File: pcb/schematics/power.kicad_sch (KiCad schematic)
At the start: 0 parts

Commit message: add more components
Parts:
- added U?: LP3853ESX-3.3/NOPB, VREG_TPS79625KTTR, symbol LP3853ESX-3.3_NOPB:LP3853ESX-3.3/NOPB
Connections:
- new net: U?.3 (GND), U?.6 (GND)
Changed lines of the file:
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@@
 (kicad_sch (version 20220126) (generator eeschema)
   (paper "A4")
+  (symbol (lib_id "LP3853ESX-3.3_NOPB:LP3853ESX-3.3{slash}NOPB") (at 148.59 86.36 0) (unit 1)
+    (in_bom yes) (on_board yes) (fields_autoplaced)
+    (property "Reference" "U?" (id 0) (at 148.59 72.39 0)
+      (effects (font (size 1.27 1.27)))
+    )
+    (property "Value" "LP3853ESX-3.3/NOPB" (id 1) (at 148.59 74.93 0)
+      (effects (font (size 1.27 1.27)))
+    )
+    (property "Footprint" "VREG_TPS79625KTTR" (id 2) (at 148.59 86.36 0)
+      (effects (font (size 1.27 1.27)) (justify left bottom) hide)
+    )
+    (property "Datasheet" "https://www.ti.com/lit/ds/symlink/lp3853.pdf?HQS=dis-mous-null-mousermode-dsf-pf-null-wwe&ts=1634641603473&ref_url=https%253A%252F%252Fcz.mouser.com%252F" (id 3) (at 148.59 86.36 0)
+      (effects (font (size 1.27 1.27)) (justify left bottom) hide)
+    )
+    (pin "1")
+    (pin "2")
+    (pin "3")
+    (pin "4")
+    (pin "5")
+    (pin "6")
+  )
 )

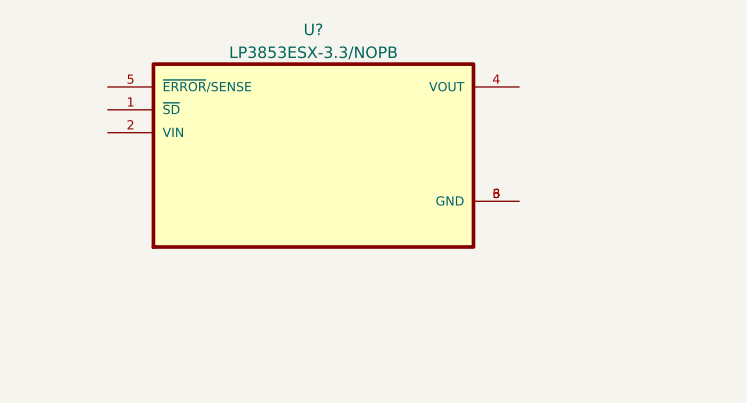
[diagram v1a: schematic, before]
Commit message: add architecture diagramé
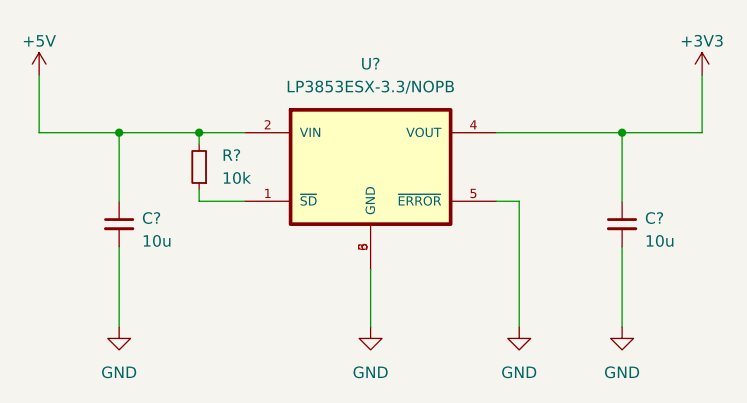
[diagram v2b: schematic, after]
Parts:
- added C? (x2): 10u, symbol Device:C_Small
- added R?: 10k, symbol Device:R_Small
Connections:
- net at U?.1 (~{SD}): now also R?.1
- net +5V: now reaches U?.2 (VIN)
- net +5V: now also C?.1, R?.2
- net GND: now reaches U?.3 (GND), U?.6 (GND)
- net GND: now also U?.5 (~{ERROR}), C?.2, C?.2
- net +3V3: now reaches U?.4 (VOUT)
- net +3V3: now also C?.1
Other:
- moved on the sheet: U?
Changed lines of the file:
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@@
 (kicad_sch (version 20220126) (generator eeschema)
   (paper "A4")
-  (symbol (lib_id "LP3853ESX-3.3_NOPB:LP3853ESX-3.3{slash}NOPB") (at 148.59 86.36 0) (unit 1)
-    (in_bom yes) (on_board yes) (fields_autoplaced)
-    (property "Reference" "U?" (id 0) (at 148.59 72.39 0)
-      (effects (font (size 1.27 1.27)))
-    )
-    (property "Value" "LP3853ESX-3.3/NOPB" (id 1) (at 148.59 74.93 0)
-      (effects (font (size 1.27 1.27)))
-    )
-    (property "Footprint" "VREG_TPS79625KTTR" (id 2) (at 148.59 86.36 0)
+  (junction (at 182.88 83.82) (diameter 0) (color 0 0 0 0)
+  )
+  (junction (at 135.89 83.82) (diameter 0) (color 0 0 0 0)
+  )
+  (junction (at 127 83.82) (diameter 0) (color 0 0 0 0)
+  )
+  (wire (pts (xy 182.88 83.82) (xy 182.88 91.44))
+    (stroke (width 0) (type default))
+  )
+  (wire (pts (xy 191.77 83.82) (xy 191.77 77.47))
+    (stroke (width 0) (type default))
+  )
+  (wire (pts (xy 118.11 77.47) (xy 118.11 83.82))
+    (stroke (width 0) (type default))
+  )
+  (wire (pts (xy 127 96.52) (xy 127 105.41))
+    (stroke (width 0) (type default))
+  )
+  (wire (pts (xy 118.11 83.82) (xy 127 83.82))
+    (stroke (width 0) (type default))
+  )
+  (wire (pts (xy 135.89 83.82) (xy 135.89 85.09))
+    (stroke (width 0) (type default))
+  )
+  (wire (pts (xy 171.45 105.41) (xy 171.45 91.44))
+    (stroke (width 0) (type default))
+  )
+  (wire (pts (xy 171.45 91.44) (xy 168.91 91.44))
+    (stroke (width 0) (type default))
+  )
+  (wire (pts (xy 182.88 96.52) (xy 182.88 105.41))
+    (stroke (width 0) (type default))
+  )
+  (wire (pts (xy 127 83.82) (xy 135.89 83.82))
+    (stroke (width 0) (type default))
+  )
+  (wire (pts (xy 140.97 91.44) (xy 135.89 91.44))
+    (stroke (width 0) (type default))
+  )
+  (wire (pts (xy 135.89 91.44) (xy 135.89 90.17))
+    (stroke (width 0) (type default))
+  )
+  (wire (pts (xy 168.91 83.82) (xy 182.88 83.82))
+    (stroke (width 0) (type default))
+  )
+  (wire (pts (xy 127 83.82) (xy 127 91.44))
+    (stroke (width 0) (type default))
+  )
+  (wire (pts (xy 182.88 83.82) (xy 191.77 83.82))
+    (stroke (width 0) (type default))
+  )
+  (wire (pts (xy 135.89 83.82) (xy 140.97 83.82))
+    (stroke (width 0) (type default))
+  )
+  (wire (pts (xy 154.94 99.06) (xy 154.94 105.41))
+    (stroke (width 0) (type default))
+  )
+  (symbol (lib_id "power:GND") (at 127 105.41 0) (unit 1)
+    (in_bom yes) (on_board yes) (fields_autoplaced)
+    (property "Reference" "#PWR?" (id 0) (at 127 111.76 0)
+      (effects (font (size 1.27 1.27)) hide)
+    )
+    (property "Value" "GND" (id 1) (at 127 110.49 0)
+      (effects (font (size 1.27 1.27)))
+    )
+    (property "Footprint" "" (id 2) (at 127 105.41 0)
+      (effects (font (size 1.27 1.27)) hide)
+    )
+    (property "Datasheet" "" (id 3) (at 127 105.41 0)
+      (effects (font (size 1.27 1.27)) hide)
+    )
+    (pin "1")
+  )
+  (symbol (lib_id "power:+5V") (at 118.11 77.47 0) (unit 1)
+    (in_bom yes) (on_board yes) (fields_autoplaced)
+    (property "Reference" "#PWR?" (id 0) (at 118.11 81.28 0)
+      (effects (font (size 1.27 1.27)) hide)
+    )
+    (property "Value" "+5V" (id 1) (at 118.11 73.66 0)
+      (effects (font (size 1.27 1.27)))
+    )
+    (property "Footprint" "" (id 2) (at 118.11 77.47 0)
+      (effects (font (size 1.27 1.27)) hide)
+    )
+    (property "Datasheet" "" (id 3) (at 118.11 77.47 0)
+      (effects (font (size 1.27 1.27)) hide)
+    )
+    (pin "1")
+  )
+  (symbol (lib_id "power:+3V3") (at 191.77 77.47 0) (unit 1)
+    (in_bom yes) (on_board yes) (fields_autoplaced)
+    (property "Reference" "#PWR?" (id 0) (at 191.77 81.28 0)
+      (effects (font (size 1.27 1.27)) hide)
+    )
+    (property "Value" "+3V3" (id 1) (at 191.77 73.66 0)
+      (effects (font (size 1.27 1.27)))
+    )
+    (property "Footprint" "" (id 2) (at 191.77 77.47 0)
+      (effects (font (size 1.27 1.27)) hide)
+    )
+    (property "Datasheet" "" (id 3) (at 191.77 77.47 0)
+      (effects (font (size 1.27 1.27)) hide)
+    )
+    (pin "1")
+  )
+  (symbol (lib_id "LP3853ESX-3.3_NOPB:LP3853ESX-3.3{slash}NOPB") (at 163.83 91.44 0) (unit 1)
+    (in_bom yes) (on_board yes)
+    (property "Reference" "U?" (id 0) (at 154.94 76.2 0)
+      (effects (font (size 1.27 1.27)))
+    )
+    (property "Value" "LP3853ESX-3.3/NOPB" (id 1) (at 154.94 78.74 0)
+      (effects (font (size 1.27 1.27)))
+    )
+    (property "Footprint" "VREG_TPS79625KTTR" (id 2) (at 163.83 91.44 0)
       (effects (font (size 1.27 1.27)) (justify left bottom) hide)
     )
-    (property "Datasheet" "https://www.ti.com/lit/ds/symlink/lp3853.pdf?HQS=dis-mous-null-mousermode-dsf-pf-null-wwe&ts=1634641603473&ref_url=https%253A%252F%252Fcz.mouser.com%252F" (id 3) (at 148.59 86.36 0)
+    (property "Datasheet" "https://www.ti.com/lit/ds/symlink/lp3853.pdf?HQS=dis-mous-null-mousermode-dsf-pf-null-wwe&ts=1634641603473&ref_url=https%253A%252F%252Fcz.mouser.com%252F" (id 3) (at 163.83 91.44 0)
       (effects (font (size 1.27 1.27)) (justify left bottom) hide)
     )
@@
     (pin "6")
   )
+  (symbol (lib_id "power:GND") (at 171.45 105.41 0) (unit 1)
+    (in_bom yes) (on_board yes) (fields_autoplaced)
+    (property "Reference" "#PWR?" (id 0) (at 171.45 111.76 0)
+      (effects (font (size 1.27 1.27)) hide)
+    )
+    (property "Value" "GND" (id 1) (at 171.45 110.49 0)
+      (effects (font (size 1.27 1.27)))
+    )
+    (property "Footprint" "" (id 2) (at 171.45 105.41 0)
+      (effects (font (size 1.27 1.27)) hide)
+    )
+    (property "Datasheet" "" (id 3) (at 171.45 105.41 0)
+      (effects (font (size 1.27 1.27)) hide)
+    )
+    (pin "1")
+  )
+  (symbol (lib_id "Device:C_Small") (at 127 93.98 0) (unit 1)
+    (in_bom yes) (on_board yes) (fields_autoplaced)
+    (property "Reference" "C?" (id 0) (at 129.54 93.3513 0)
+      (effects (font (size 1.27 1.27)) (justify left))
+    )
+    (property "Value" "10u" (id 1) (at 129.54 95.8913 0)
+      (effects (font (size 1.27 1.27)) (justify left))
+    )
+    (property "Footprint" "" (id 2) (at 127 93.98 0)
+      (effects (font (size 1.27 1.27)) hide)
+    )
+    (property "Datasheet" "~" (id 3) (at 127 93.98 0)
+      (effects (font (size 1.27 1.27)) hide)
+    )
+    (pin "1")
+    (pin "2")
+  )
+  (symbol (lib_id "Device:R_Small") (at 135.89 87.63 180) (unit 1)
+    (in_bom yes) (on_board yes)
+    (property "Reference" "R?" (id 0) (at 138.43 86.36 0)
+      (effects (font (size 1.27 1.27)) (justify right))
+    )
+    (property "Value" "10k" (id 1) (at 138.43 88.9 0)
+      (effects (font (size 1.27 1.27)) (justify right))
+    )
+    (property "Footprint" "" (id 2) (at 135.89 87.63 0)
+      (effects (font (size 1.27 1.27)) hide)
+    )
+    (property "Datasheet" "~" (id 3) (at 135.89 87.63 0)
+      (effects (font (size 1.27 1.27)) hide)
+    )
+    (pin "1")
+    (pin "2")
+  )
+  (symbol (lib_id "power:GND") (at 154.94 105.41 0) (unit 1)
+    (in_bom yes) (on_board yes) (fields_autoplaced)
+    (property "Reference" "#PWR?" (id 0) (at 154.94 111.76 0)
+      (effects (font (size 1.27 1.27)) hide)
+    )
+    (property "Value" "GND" (id 1) (at 154.94 110.49 0)
+      (effects (font (size 1.27 1.27)))
+    )
+    (property "Footprint" "" (id 2) (at 154.94 105.41 0)
+      (effects (font (size 1.27 1.27)) hide)
+    )
+    (property "Datasheet" "" (id 3) (at 154.94 105.41 0)
+      (effects (font (size 1.27 1.27)) hide)
+    )
+    (pin "1")
+  )
+  (symbol (lib_id "Device:C_Small") (at 182.88 93.98 0) (unit 1)
+    (in_bom yes) (on_board yes) (fields_autoplaced)
+    (property "Reference" "C?" (id 0) (at 185.42 93.3513 0)
+      (effects (font (size 1.27 1.27)) (justify left))
+    )
+    (property "Value" "10u" (id 1) (at 185.42 95.8913 0)
+      (effects (font (size 1.27 1.27)) (justify left))
+    )
+    (property "Footprint" "" (id 2) (at 182.88 93.98 0)
+      (effects (font (size 1.27 1.27)) hide)
+    )
+    (property "Datasheet" "~" (id 3) (at 182.88 93.98 0)
+      (effects (font (size 1.27 1.27)) hide)
+    )
+    (pin "1")
+    (pin "2")
+  )
+  (symbol (lib_id "power:GND") (at 182.88 105.41 0) (unit 1)
+    (in_bom yes) (on_board yes) (fields_autoplaced)
+    (property "Reference" "#PWR?" (id 0) (at 182.88 111.76 0)
+      (effects (font (size 1.27 1.27)) hide)
+    )
+    (property "Value" "GND" (id 1) (at 182.88 110.49 0)
+      (effects (font (size 1.27 1.27)))
+    )
+    (property "Footprint" "" (id 2) (at 182.88 105.41 0)
+      (effects (font (size 1.27 1.27)) hide)
+    )
+    (property "Datasheet" "" (id 3) (at 182.88 105.41 0)
+      (effects (font (size 1.27 1.27)) hide)
+    )
+    (pin "1")
+  )
 )

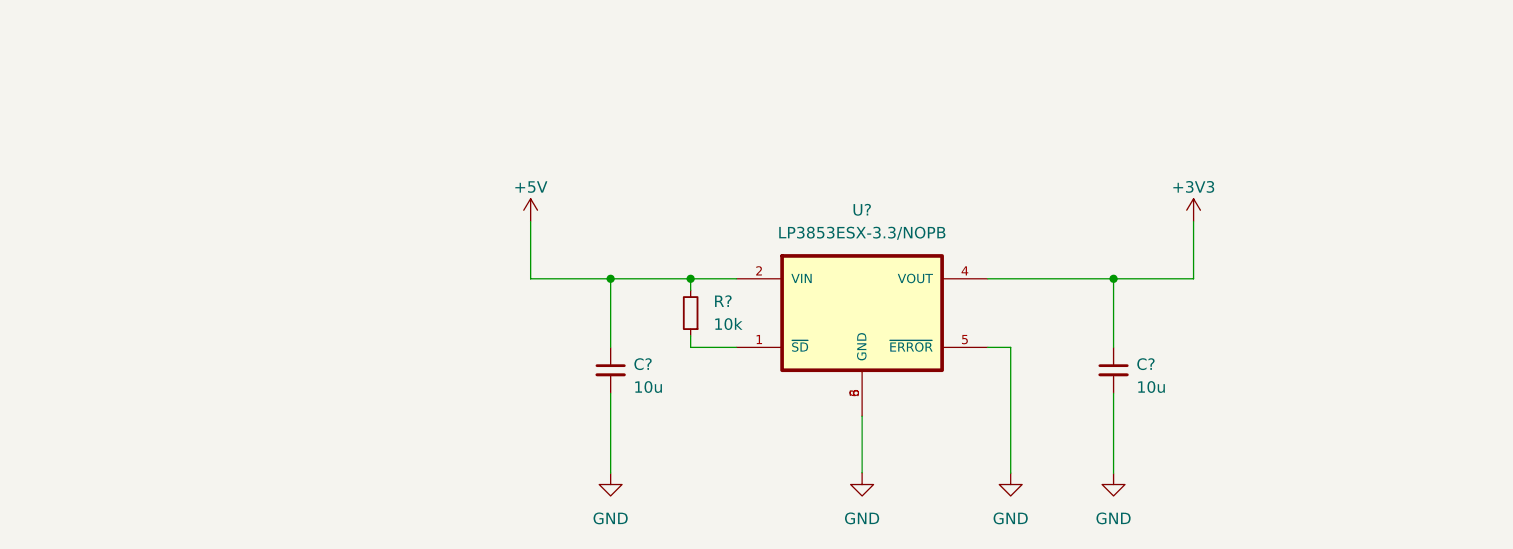
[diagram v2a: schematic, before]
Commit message: start adding decoupling caps for the hdmi frontend
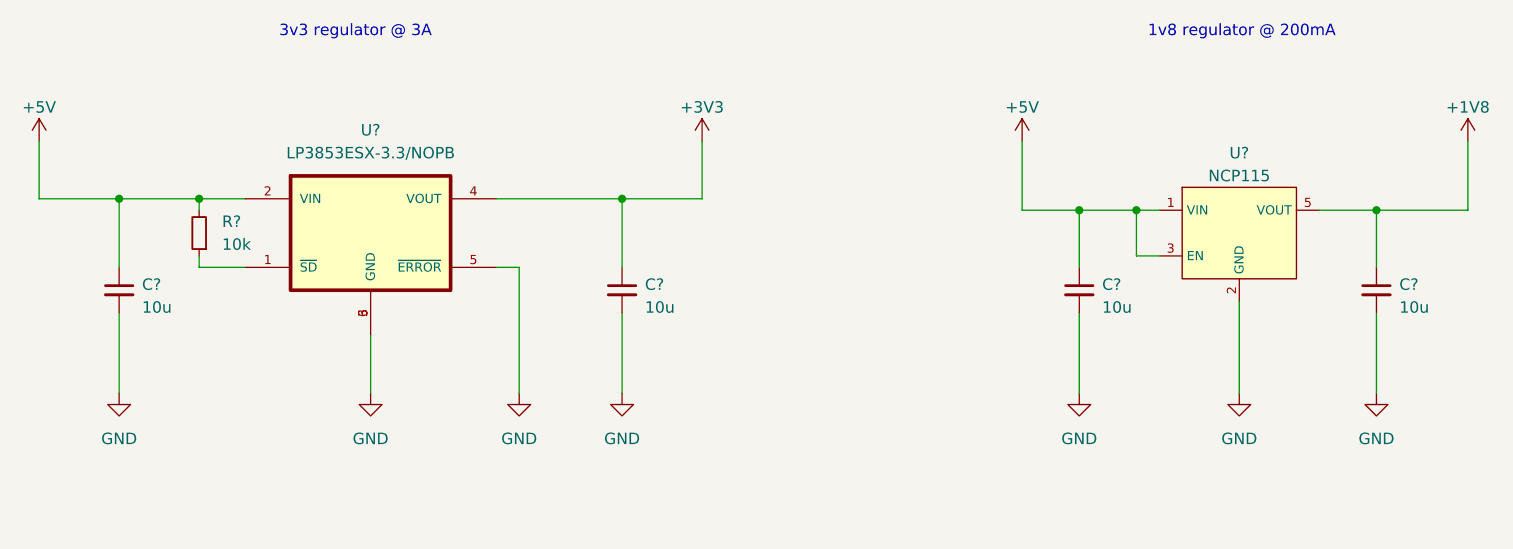
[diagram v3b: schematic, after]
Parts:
- added C? (x2): 10u, symbol Device:C_Small
- added U?: NCP115, Package_DFN_QFN:OnSemi_XDFN4-1EP_1.0x1.0mm_EP0.52x0.52mm, symbol NCP115:NCP115
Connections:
- net +5V: now also C?.1, U?.1 (VIN), U?.3 (EN)
- net GND: now also C?.2, C?.2, U?.2 (GND)
- new net +1V8: C?.1, U?.5 (VOUT)
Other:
- note added: "1v8 regulator @ 200mA"
- note added: "3v3 regulator @ 3A"
- moved on the sheet: C?, R?, U?
